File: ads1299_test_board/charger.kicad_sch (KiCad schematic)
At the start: 8 parts, among them Q1 AO3407A, U2 MCP73832-2-OT

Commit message: 27/05
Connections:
- net Vout renamed +BATT
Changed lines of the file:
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@@
 		)
 	)
-	(hierarchical_label "Vout"
+	(hierarchical_label "+BATT"
 		(shape output)
 		(at 77.47 60.96 270)

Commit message: charger circuit
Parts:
- added F1: Fuse, symbol Device:Fuse
- added J1: Conn_01x02, symbol Connector_Generic:Conn_01x02
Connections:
- net +BATT is gone; now on net Vbat: Q1.3 (D)
- net Vbat: now also F1.1
- net agnd renamed GND
- net GND: now also J1.1 (Pin_1)
- new net: F1.2, J1.2 (Pin_2)

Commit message: usb, esp32 s3 wroom 1
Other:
- moved on the sheet: C12, C13, D1, F1, J1, Q1, R10, R11, R9, U2

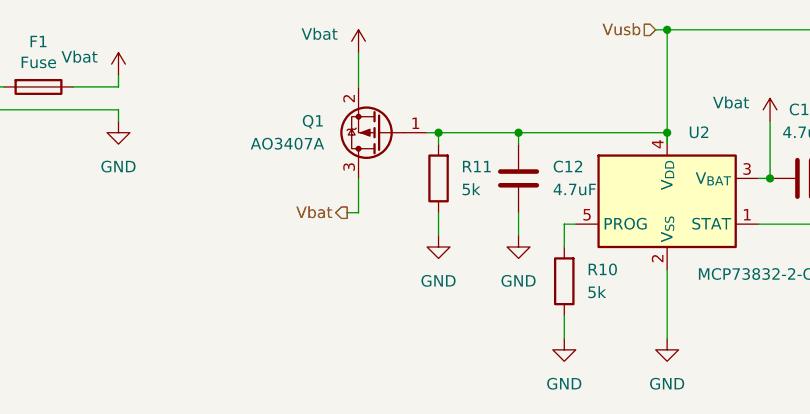
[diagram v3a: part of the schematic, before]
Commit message: usb charge and power circuit switch
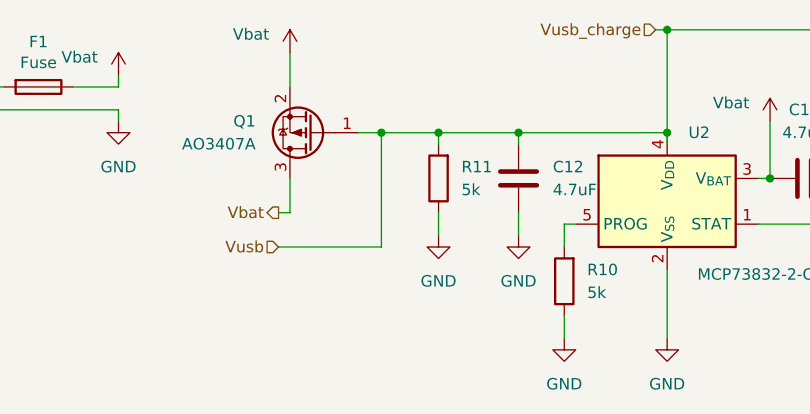
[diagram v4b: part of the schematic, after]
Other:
- moved on the sheet: Q1
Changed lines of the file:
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@@
 	(paper "A4")
+	(junction
+		(at 154.94 95.25)
+		(diameter 0)
+		(color 0 0 0 0)
+	)
+	(junction
+		(at 182.88 100.33)
+		(diameter 0)
+		(color 0 0 0 0)
+	)
+	(junction
+		(at 171.45 83.82)
+		(diameter 0)
+		(color 0 0 0 0)
+	)
+	(junction
+		(at 139.7 95.25)
+		(diameter 0)
+		(color 0 0 0 0)
+	)
 	(junction
 		(at 146.05 95.25)
@@
 	)
 	(junction
-		(at 154.94 95.25)
-		(diameter 0)
-		(color 0 0 0 0)
-	)
-	(junction
-		(at 182.88 100.33)
-		(diameter 0)
-		(color 0 0 0 0)
-	)
-	(junction
-		(at 171.45 83.82)
-		(diameter 0)
-		(color 0 0 0 0)
-	)
-	(junction
 		(at 171.45 95.25)
 		(diameter 0)
@@
 	(wire
 		(pts
+			(xy 139.7 95.25) (xy 146.05 95.25)
+		)
+		(stroke
+			(width 0)
+			(type default)
+		)
+	)
+	(wire
+		(pts
 			(xy 96.52 92.71) (xy 110.49 92.71)
 		)
@@
 	(wire
 		(pts
-			(xy 137.16 100.33) (xy 137.16 104.14)
+			(xy 129.54 100.33) (xy 129.54 104.14)
 		)
 		(stroke
@@
 	(wire
 		(pts
+			(xy 139.7 107.95) (xy 139.7 95.25)
+		)
+		(stroke
+			(width 0)
+			(type default)
+		)
+	)
+	(wire
+		(pts
 			(xy 105.41 90.17) (xy 110.49 90.17)
 		)
@@
 	(wire
 		(pts
-			(xy 137.16 104.14) (xy 135.89 104.14)
+			(xy 129.54 104.14) (xy 128.27 104.14)
+		)
+		(stroke
+			(width 0)
+			(type default)
+		)
+	)
+	(wire
+		(pts
+			(xy 128.27 107.95) (xy 139.7 107.95)
 		)
 		(stroke
@@
 	(wire
 		(pts
-			(xy 144.78 95.25) (xy 146.05 95.25)
+			(xy 137.16 95.25) (xy 139.7 95.25)
 		)
 		(stroke
@@
 	(wire
 		(pts
-			(xy 137.16 86.36) (xy 137.16 90.17)
+			(xy 129.54 86.36) (xy 129.54 90.17)
 		)
 		(stroke
@@
 		)
 	)
-	(hierarchical_label "Vbat"
-		(shape output)
-		(at 135.89 104.14 180)
+	(hierarchical_label "Vusb"
+		(shape input)
+		(at 128.27 107.95 180)
 		(effects
 			(font
@@
 		)
 	)
-	(hierarchical_label "Vusb"
+	(hierarchical_label "Vbat"
+		(shape output)
+		(at 128.27 104.14 180)
+		(effects
+			(font
+				(size 1.27 1.27)
+			)
+			(justify right)
+		)
+	)
+	(hierarchical_label "Vusb_charge"
 		(shape input)
 		(at 170.18 83.82 180)
@@
 	(symbol
 		(lib_id "power:+BATT")
-		(at 137.16 86.36 0)
+		(at 129.54 86.36 0)
 		(unit 1)
 		(body_style 1)
@@
 		(dnp no)
 		(property "Reference" "#PWR016"
-			(at 137.16 90.17 0)
+			(at 129.54 90.17 0)
 			(hide yes)
 			(show_name no)
@@
 		)
 		(property "Value" "Vbat"
-			(at 132.842 84.328 0)
+			(at 125.222 84.328 0)
 			(show_name no)
 			(do_not_autoplace no)
@@
 		)
 		(property "Footprint" ""
-			(at 137.16 86.36 0)
+			(at 129.54 86.36 0)
 			(hide yes)
 			(show_name no)
@@
 		)
 		(property "Datasheet" ""
-			(at 137.16 86.36 0)
+			(at 129.54 86.36 0)
 			(hide yes)
 			(show_name no)
@@
 		)
 		(property "Description" "Power symbol creates a global label with name \"+BATT\""
-			(at 137.16 86.36 0)
+			(at 129.54 86.36 0)
 			(hide yes)
 			(show_name no)
@@
 	(symbol
 		(lib_id "Transistor_FET:AO3401A")
-		(at 139.7 95.25 180)
+		(at 132.08 95.25 180)
 		(unit 1)
 		(body_style 1)
@@
 		(fields_autoplaced yes)
 		(property "Reference" "Q1"
-			(at 133.35 93.9799 0)
+			(at 125.73 93.9799 0)
 			(show_name no)
 			(do_not_autoplace no)
@@
 		)
 		(property "Value" "AO3407A"
-			(at 133.35 96.5199 0)
+			(at 125.73 96.5199 0)
 			(show_name no)
 			(do_not_autoplace no)
@@
 		)
 		(property "Footprint" "Package_TO_SOT_SMD:SOT-23"
-			(at 134.62 93.345 0)
+			(at 127 93.345 0)
 			(hide yes)
 			(show_name no)
@@
 		)
 		(property "Datasheet" "http://www.aosmd.com/pdfs/datasheet/AO3401A.pdf"
-			(at 134.62 91.44 0)
+			(at 127 91.44 0)
 			(hide yes)
 			(show_name no)
@@
 		)
 		(property "Description" "-4.0A Id, -30V Vds, P-Channel MOSFET, SOT-23"
-			(at 139.7 95.25 0)
-			(hide yes)
-			(show_name no)
+			(at 132.08 95.25 0)
+			(hide yes)
+			(show_name no)

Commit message: GPIO, SRB
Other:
- moved on the sheet: C12, C13, D1, F1, J1, Q1, R10, R11, R9, U2

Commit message: updates
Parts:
- added D2: 1N4448W, Diode_SMD:D_SOD-123, symbol Diode:1N4448W
- C12, C13, R10, R11: footprint (none) -> Capacitor_SMD:C_0402_1005Metric_Pad0.74x0.62mm_HandSolder
- D1: footprint (none) -> LED_SMD:LED_0603_1608Metric
- J1: footprint (none) -> Connector_JST:JST_EH_B2B-EH-A_1x02_P2.50mm_Vertical
- R9: value 470 -> 330; footprint (none) -> Capacitor_SMD:C_0402_1005Metric_Pad0.74x0.62mm_HandSolder
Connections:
- net Vusb: now also D2.1 (K); no longer C12.1, D1.2 (A), R11.2, U2.4 (V_{DD})
- new net Vusb_charge: C12.1, D1.2 (A), D2.2 (A), R11.2, U2.4 (V_{DD})
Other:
- moved on the sheet: F1, J1, Q1

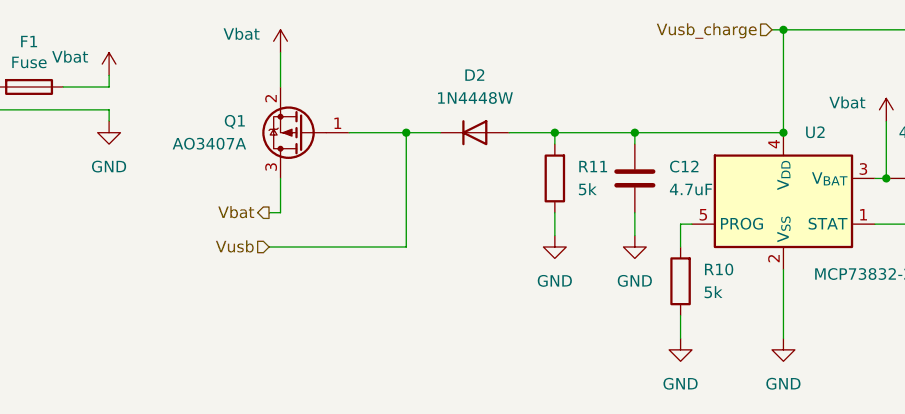
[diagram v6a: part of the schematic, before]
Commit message: fixed Vbat net name
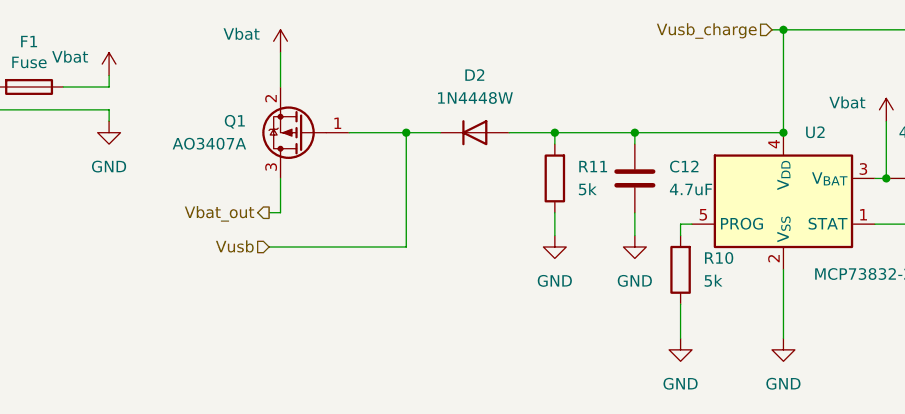
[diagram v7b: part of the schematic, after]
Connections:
- net Vbat: no longer Q1.3 (D)
- new net Vbat_out: Q1.3 (D)
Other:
- moved on the sheet: R10
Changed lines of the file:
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@@
 	(wire
 		(pts
-			(xy 156.21 101.6) (xy 156.21 99.06)
+			(xy 156.21 100.33) (xy 156.21 99.06)
 		)
 		(stroke
@@
 	(wire
 		(pts
-			(xy 156.21 109.22) (xy 156.21 111.76)
+			(xy 156.21 107.95) (xy 156.21 111.76)
 		)
 		(stroke
@@
 		)
 	)
-	(hierarchical_label "Vbat"
+	(hierarchical_label "Vbat_out"
 		(shape output)
 		(at 110.49 97.79 180)
@@
 	(symbol
 		(lib_id "Device:R")
-		(at 156.21 105.41 180)
+		(at 156.21 104.14 180)
 		(unit 1)
 		(body_style 1)
@@
 		(fields_autoplaced yes)
 		(property "Reference" "R10"
-			(at 158.75 104.1399 0)
+			(at 158.75 102.8699 0)
 			(show_name no)
 			(do_not_autoplace no)
@@
 		)
 		(property "Value" "5k"
-			(at 158.75 106.6799 0)
+			(at 158.75 105.4099 0)
 			(show_name no)
 			(do_not_autoplace no)
@@
 		)
 		(property "Footprint" "Capacitor_SMD:C_0402_1005Metric_Pad0.74x0.62mm_HandSolder"
-			(at 157.988 105.41 90)
+			(at 157.988 104.14 90)
 			(hide yes)
 			(show_name no)
@@
 		)
 		(property "Datasheet" ""
-			(at 156.21 105.41 0)
+			(at 156.21 104.14 0)
 			(hide yes)
 			(show_name no)
@@
 		)
 		(property "Description" "Resistor"
-			(at 156.21 105.41 0)
-			(hide yes)
-			(show_name no)
+			(at 156.21 104.14 0)
+			(hide yes)
+			(show_name no)
